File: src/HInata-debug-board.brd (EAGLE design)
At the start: 7 parts

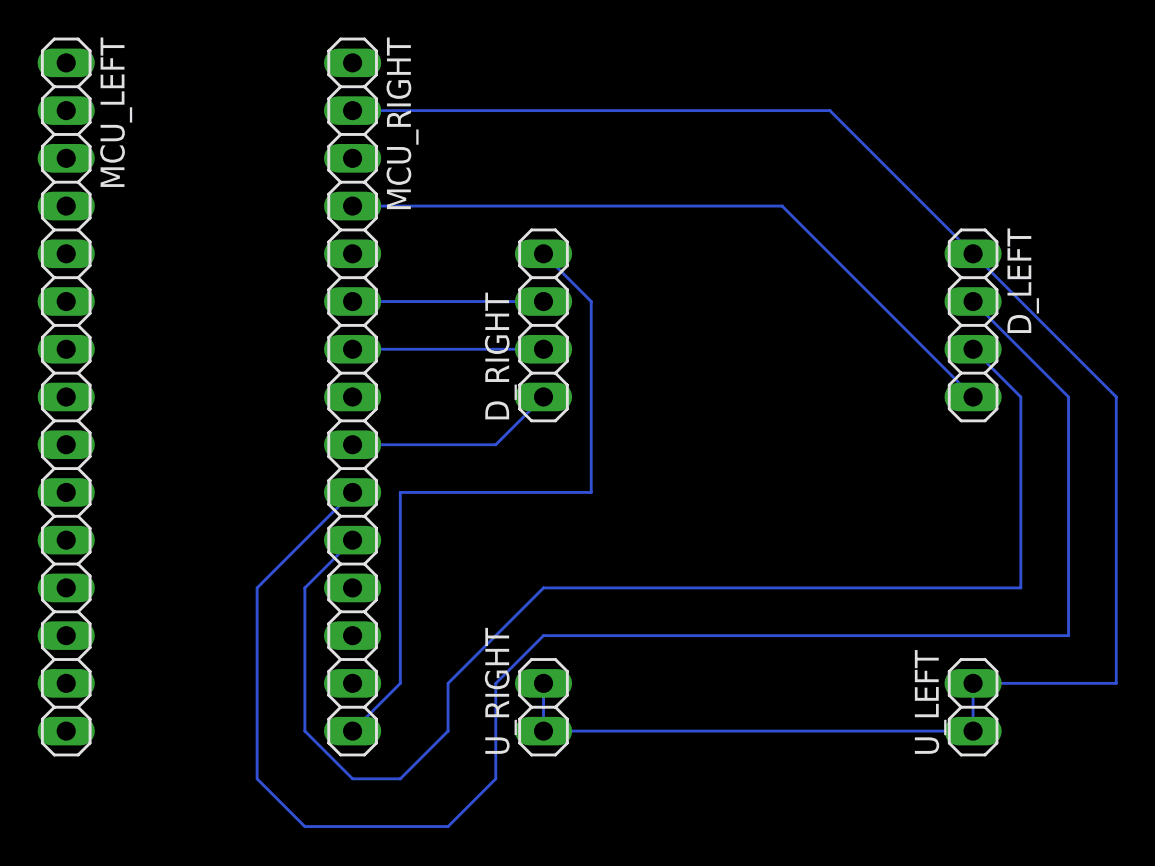
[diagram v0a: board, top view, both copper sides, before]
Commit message: fix Hinata-debug-board配線
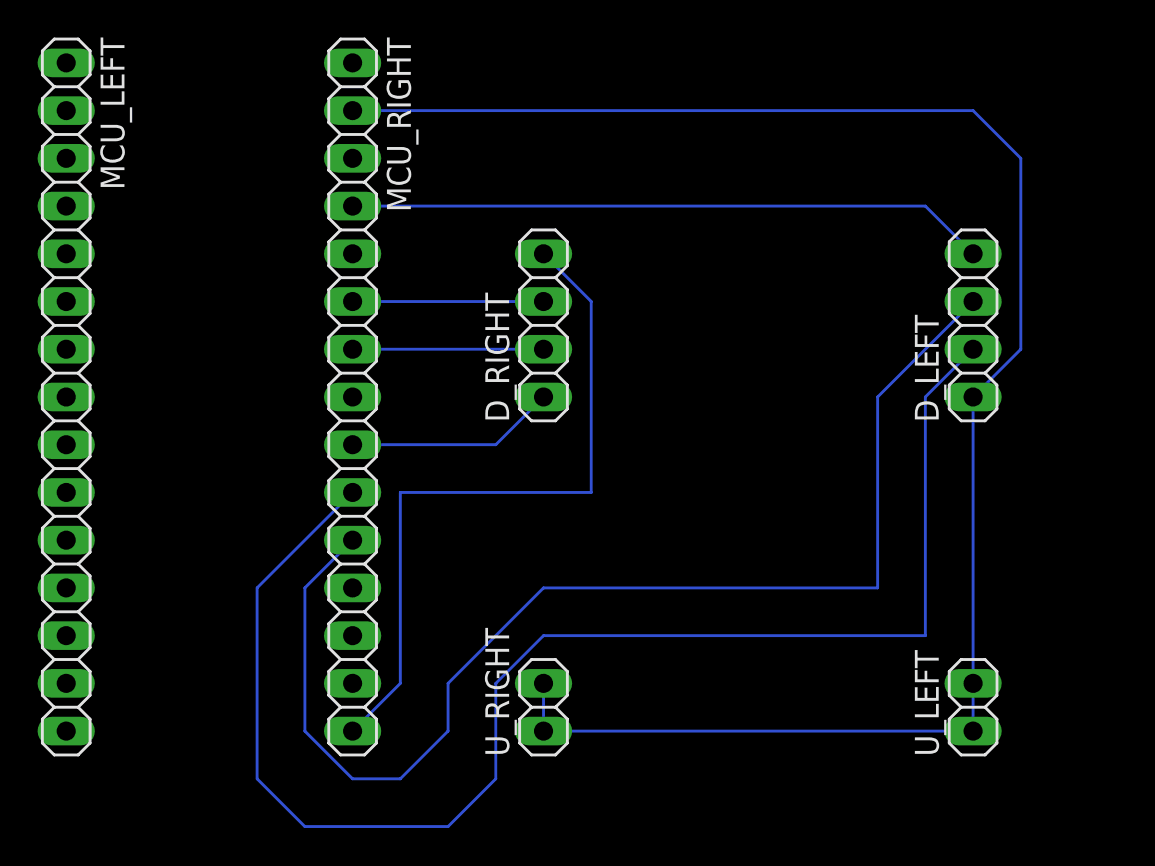
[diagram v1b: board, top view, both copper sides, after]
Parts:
- turned D_LEFT to 90 degrees
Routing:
- net INT: track 88.6 -> 77.4 mm
- net GND: track 97.8 -> 93.5 mm
- net COM_LED: track 69.8 -> 65.8 mm
- net 5V: track 37.2 -> 34.1 mm
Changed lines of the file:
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@@
 </autorouter>
 <elements>
-<element name="D_LEFT" library="pinhead" library_urn="urn:adsk.eagle:library:325" package="1X04" package3d_urn="urn:adsk.eagle:package:22407/2" value="" x="62.23" y="30.48" smashed="yes" rot="R270">
-<attribute name="NAME" x="64.0588" y="35.6362" size="1.27" layer="25" ratio="10" rot="R270"/>
-<attribute name="POPULARITY" value="91" x="46.99" y="11.43" size="1.778" layer="27" rot="R270" display="off"/>
-<attribute name="VALUE" x="59.055" y="35.56" size="1.27" layer="27" rot="R270"/>
+<element name="D_LEFT" library="pinhead" library_urn="urn:adsk.eagle:library:325" package="1X04" package3d_urn="urn:adsk.eagle:package:22407/2" value="" x="62.23" y="30.48" smashed="yes" rot="R90">
+<attribute name="NAME" x="60.4012" y="25.3238" size="1.27" layer="25" ratio="10" rot="R90"/>
+<attribute name="POPULARITY" value="91" x="77.47" y="49.53" size="1.778" layer="27" rot="R90" display="off"/>
+<attribute name="VALUE" x="65.405" y="25.4" size="1.27" layer="27" rot="R90"/>
 </element>
 <element name="D_RIGHT" library="pinhead" library_urn="urn:adsk.eagle:library:325" package="1X04" package3d_urn="urn:adsk.eagle:package:22407/2" value="" x="39.37" y="30.48" smashed="yes" rot="R90">
@@
 <contactref element="MCU_RIGHT" pad="10"/>
 <contactref element="D_LEFT" pad="2"/>
-<wire x1="62.23" y1="31.75" x2="67.31" y2="26.67" width="0.1524" layer="16"/>
-<wire x1="67.31" y1="26.67" x2="67.31" y2="13.97" width="0.1524" layer="16"/>
-<wire x1="67.31" y1="13.97" x2="39.37" y2="13.97" width="0.1524" layer="16"/>
+<wire x1="59.69" y1="13.97" x2="39.37" y2="13.97" width="0.1524" layer="16"/>
 <wire x1="39.37" y1="13.97" x2="36.83" y2="11.43" width="0.1524" layer="16"/>
 <wire x1="36.83" y1="11.43" x2="36.83" y2="6.35" width="0.1524" layer="16"/>
@@
 <wire x1="29.21" y1="21.59" x2="24.13" y2="16.51" width="0.1524" layer="16"/>
 <wire x1="24.13" y1="16.51" x2="24.13" y2="6.35" width="0.1524" layer="16"/>
+<wire x1="62.23" y1="29.21" x2="59.69" y2="26.67" width="0.1524" layer="16"/>
+<wire x1="59.69" y1="26.67" x2="59.69" y2="13.97" width="0.1524" layer="16"/>
 </signal>
 <signal name="COM_LED">
@@
 <wire x1="31.75" y1="6.35" x2="34.29" y2="8.89" width="0.1524" layer="16"/>
 <wire x1="34.29" y1="8.89" x2="34.29" y2="11.43" width="0.1524" layer="16"/>
-<wire x1="34.29" y1="11.43" x2="39.37" y2="16.51" width="0.1524" layer="16"/>
-<wire x1="39.37" y1="16.51" x2="64.77" y2="16.51" width="0.1524" layer="16"/>
-<wire x1="64.77" y1="16.51" x2="64.77" y2="26.67" width="0.1524" layer="16"/>
-<wire x1="64.77" y1="26.67" x2="62.23" y2="29.21" width="0.1524" layer="16"/>
+<wire x1="39.37" y1="16.51" x2="34.29" y2="11.43" width="0.1524" layer="16"/>
+<wire x1="57.15" y1="26.67" x2="57.15" y2="16.51" width="0.1524" layer="16"/>
+<wire x1="57.15" y1="16.51" x2="39.37" y2="16.51" width="0.1524" layer="16"/>
+<wire x1="62.23" y1="31.75" x2="57.15" y2="26.67" width="0.1524" layer="16"/>
 </signal>
 <signal name="GND">
@@
 <wire x1="62.23" y1="8.89" x2="39.37" y2="8.89" width="0.1524" layer="16"/>
 <wire x1="62.23" y1="8.89" x2="62.23" y2="11.43" width="0.1524" layer="16"/>
-<wire x1="62.23" y1="34.29" x2="54.61" y2="41.91" width="0.1524" layer="16"/>
-<wire x1="54.61" y1="41.91" x2="29.21" y2="41.91" width="0.1524" layer="16"/>
-<wire x1="62.23" y1="11.43" x2="69.85" y2="11.43" width="0.1524" layer="16"/>
-<wire x1="69.85" y1="11.43" x2="69.85" y2="26.67" width="0.1524" layer="16"/>
-<wire x1="69.85" y1="26.67" x2="62.23" y2="34.29" width="0.1524" layer="16"/>
+<wire x1="62.23" y1="26.67" x2="62.23" y2="11.43" width="0.1524" layer="16"/>
+<wire x1="62.23" y1="26.67" x2="64.77" y2="29.21" width="0.1524" layer="16"/>
+<wire x1="64.77" y1="29.21" x2="64.77" y2="39.37" width="0.1524" layer="16"/>
+<wire x1="64.77" y1="39.37" x2="62.23" y2="41.91" width="0.1524" layer="16"/>
+<wire x1="62.23" y1="41.91" x2="29.21" y2="41.91" width="0.1524" layer="16"/>
 </signal>
 <signal name="5V">
 <contactref element="MCU_RIGHT" pad="4"/>
 <contactref element="D_LEFT" pad="4"/>
-<wire x1="62.23" y1="26.67" x2="52.07" y2="36.83" width="0.1524" layer="16"/>
-<wire x1="52.07" y1="36.83" x2="29.21" y2="36.83" width="0.1524" layer="16"/>
+<wire x1="62.23" y1="34.29" x2="59.69" y2="36.83" width="0.1524" layer="16"/>
+<wire x1="59.69" y1="36.83" x2="29.21" y2="36.83" width="0.1524" layer="16"/>
 </signal>
 </signals>
